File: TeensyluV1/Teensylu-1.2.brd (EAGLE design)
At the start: 101.6 x 76.2 mm, 101 parts, among them J1 M02POLAR, J11 M02POLAR, J12 M02POLAR, J2 MICROSD, J3 USB-MICRO-PTH, J4 M02POLAR, J5 4P-TERM-BLOCK284391-4, J6 39-29-3066, J7 HOTEND-1, J8 2x7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

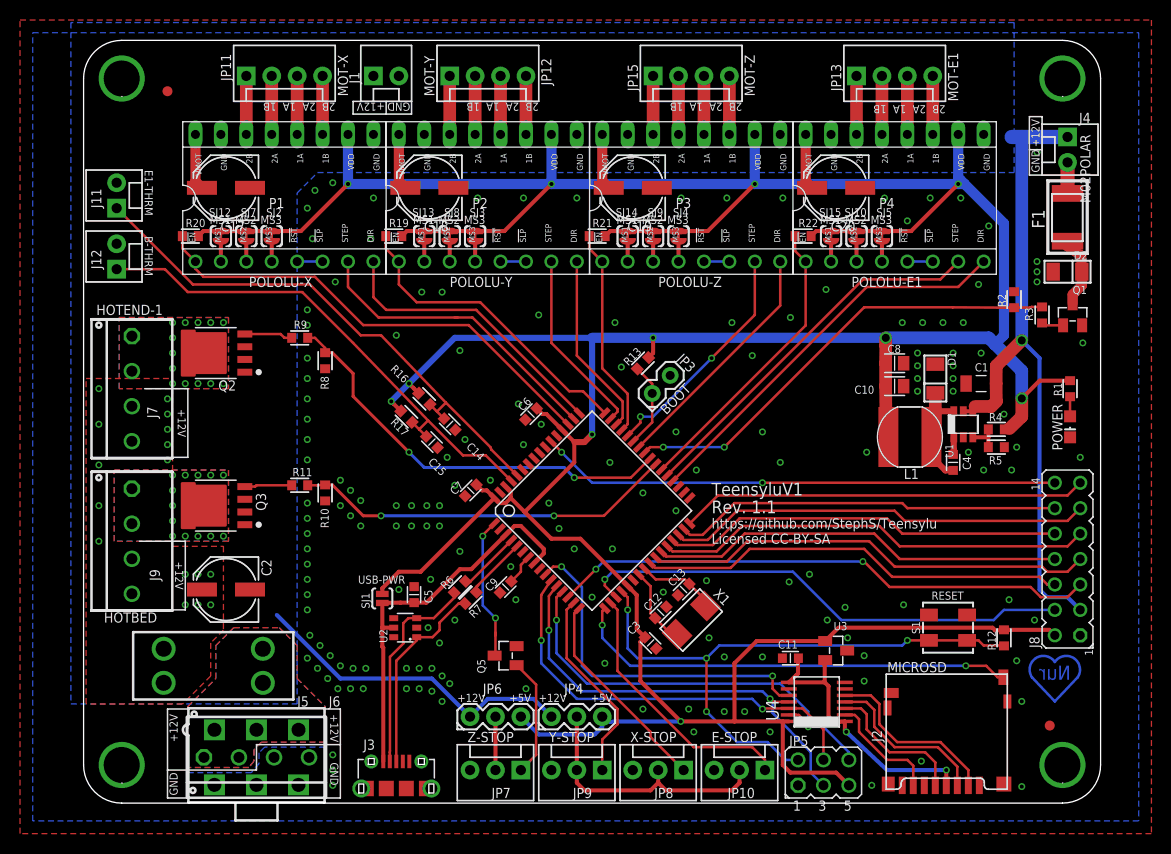
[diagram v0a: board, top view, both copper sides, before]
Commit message: Now with 4 layers!
The board is now 4 layers. This is to allow high current through the
planes. It also means less via's.
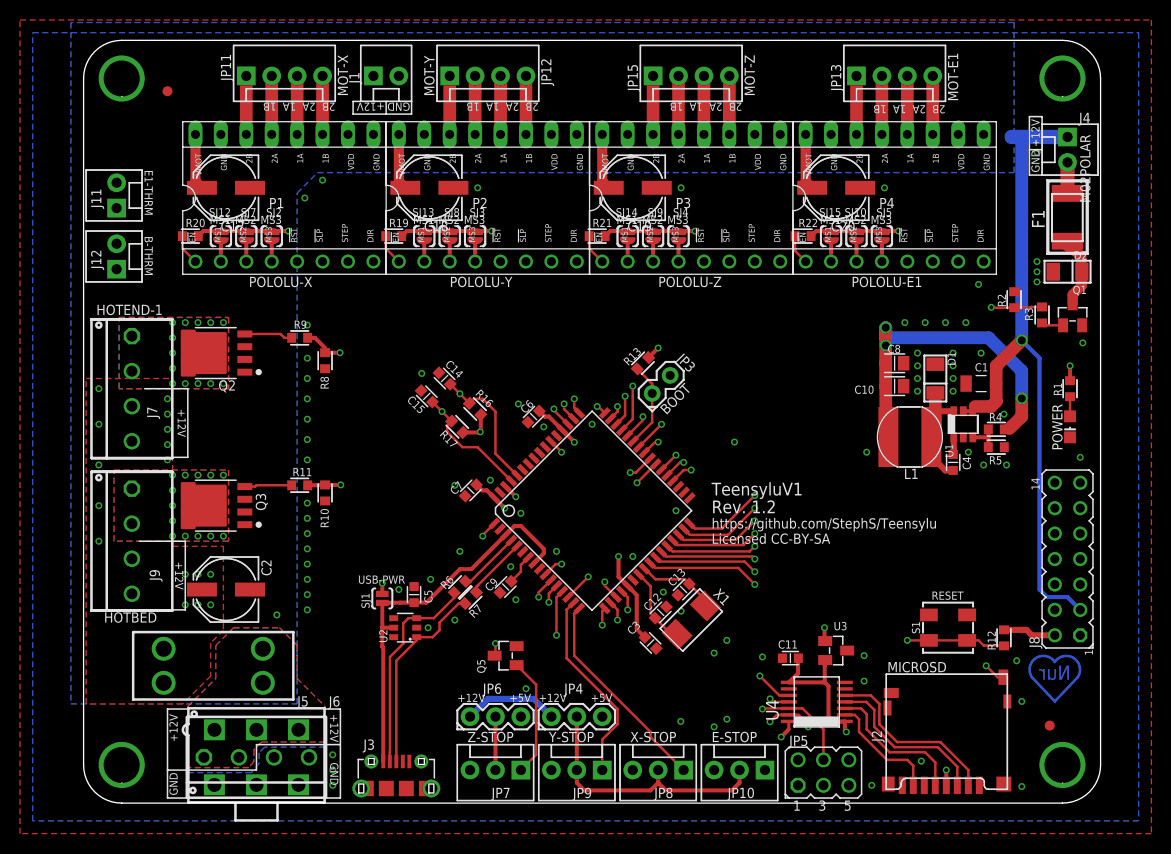
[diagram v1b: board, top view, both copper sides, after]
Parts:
- moved R16 5.18 mm to (39.1, 39.4), turned to 315 degrees
- moved R17 5.18 mm to (37.3, 37.6), turned to 315 degrees
- moved C14 4.60 mm to (36.1, 42.4), turned to 315 degrees
- moved C15 4.60 mm to (34.3, 40.6), turned to 315 degrees
- moved C6 0.36 mm to (45.0, 38.6)
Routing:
- net 5V: track 422.6 -> 107.1 mm, vias 11 -> 19
- net MISO: track 44.0 -> 40.2 mm, vias 2 -> 3
- net !RESET: track 61.4 -> 57.8 mm
- net MOSI: track 44.1 -> 40.9 mm
- net SCLK: track 42.6 -> 39.7 mm
- net SDCS: track 35.3 -> 32.4 mm
- net PD2-RX1: track 41.5 -> 39.6 mm, vias 0 -> 1
- net !HOTEND-1: track 42.4 -> 40.6 mm
- net PD1-SDA: track 45.2 -> 43.5 mm, vias 0 -> 1
- net PD3-TX1: track 43.9 -> 42.2 mm, vias 0 -> 1
- net PD0-SCL: track 42.9 -> 41.3 mm, vias 0 -> 1
- net !HOTBED: track 38.2 -> 36.7 mm
- net E-STOP: track 26.5 -> 27.9 mm, vias 0 -> 3
- net PD4: track 40.1 -> 38.8 mm, vias 0 -> 1
- net PE5: track 49.9 -> 48.7 mm
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- added copper zone on layer 15, net 12V
- added copper zone on layer 2, net 12V
- added copper zone on layer 15, net 5V
- added copper zone on layer 15, net GND
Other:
- board text added: "Rev. 1.2"
- board text removed: "Rev. 1.1"
